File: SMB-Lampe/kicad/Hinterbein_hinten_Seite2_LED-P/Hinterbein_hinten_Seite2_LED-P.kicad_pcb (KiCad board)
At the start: 2 copper layers, 13.3 x 39.6 mm, 6 parts, among them J1 Conn_01x01_Pin

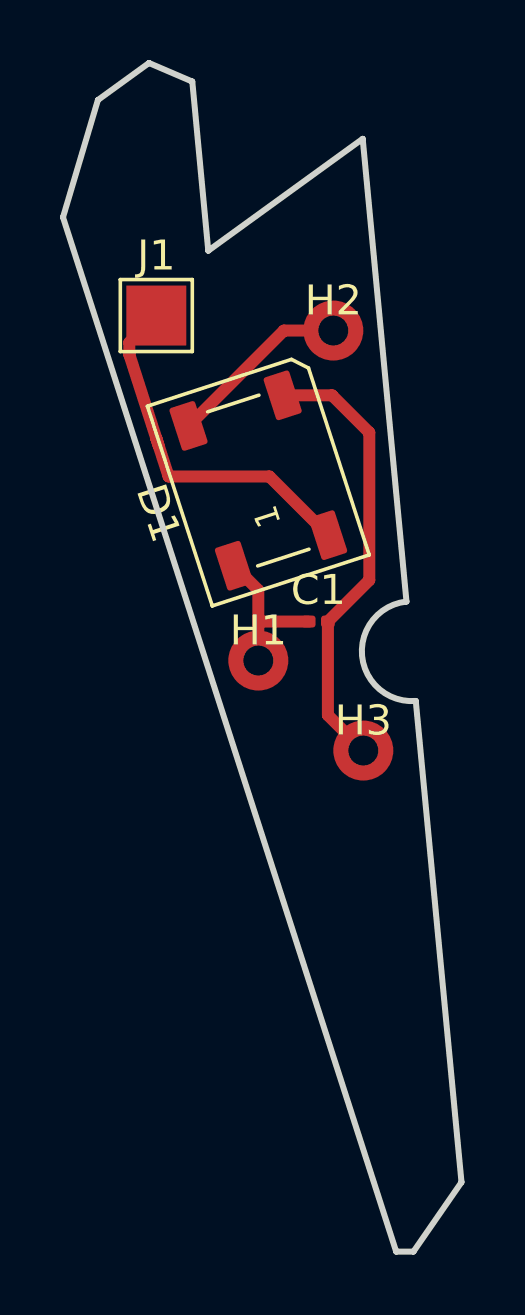
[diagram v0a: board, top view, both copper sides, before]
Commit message: Vorderes Hinterbein fertig
Alle Platinen sind fertig beschaltet
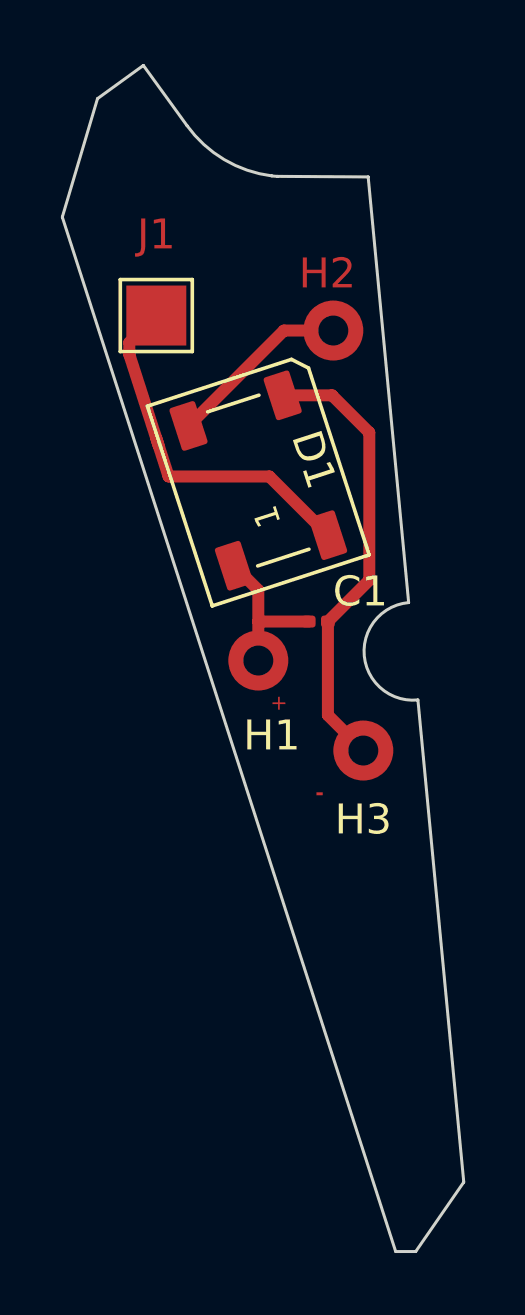
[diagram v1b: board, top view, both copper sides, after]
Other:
- board size 13.3 x 39.6 mm -> 13.4 x 39.5 mm
- board text added: "+"
- board text added: "-"
- board text removed: "108"
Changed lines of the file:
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@@
 		(at 135.5 100.7)
 		(property "Reference" "H3"
-			(at 0 -1 0)
+			(at 0 2.3 0)
 			(unlocked yes)
 			(layer "F.SilkS")
@@
 		(tags "LED RGB NeoPixel PLCC-4 5050")
 		(property "Reference" "D1"
-			(at 0 -3.5 108)
+			(at 0.094058 1.975766 108)
 			(layer "F.SilkS")
 			(effects
@@
 		)
 		(fp_line
-			(start 3.5 2.3)
+			(start 3.5 2.300001)
 			(end 3.5 -2.75)
 			(stroke
@@
 		(fp_line
 			(start 3.05 2.749999)
-			(end 3.5 2.3)
+			(end 3.5 2.300001)
 			(stroke
 				(width 0.12)
@@
 		(at 132 97.7)
 		(property "Reference" "H1"
-			(at 0 -1 0)
+			(at 0.45 2.5 0)
 			(unlocked yes)
 			(layer "F.SilkS")
@@
 		(at 134.5 86.7)
 		(property "Reference" "H2"
-			(at 0 -1 0)
-			(unlocked yes)
-			(layer "F.SilkS")
+			(at -0.2 -1.9 0)
+			(unlocked yes)
+			(layer "F.Cu")
 			(effects
 				(font
@@
 		(tags "test point SMD pad rectangle square")
 		(property "Reference" "J1"
-			(at 0 -1.998 0)
-			(layer "F.SilkS")
+			(at 0 -2.7 0)
+			(layer "F.Cu")
 			(effects
 				(font
@@
 		(tags "capacitor")
 		(property "Reference" "C1"
-			(at 0 -1.05 0)
+			(at 1.4 -1 0)
 			(layer "F.SilkS")
 			(effects
@@
 		)
 	)
-	(gr_line
-		(start 130.331995 84.039152)
-		(end 129.8 78.4)
-		(stroke
-			(width 0.2)
+	(gr_arc
+		(start 132.450996 81.545317)
+		(mid 130.861045 81.000051)
+		(end 129.620705 79.865664)
+		(stroke
+			(width 0.1)
 			(type default)
 		)
@@
 	)
 	(gr_line
-		(start 125.489765 82.924183)
-		(end 136.595866 117.402629)
-		(stroke
-			(width 0.2)
+		(start 137.247196 117.399211)
+		(end 138.848769 115.086383)
+		(stroke
+			(width 0.1)
 			(type default)
 		)
@@
 	)
 	(gr_line
-		(start 136.939186 95.734062)
-		(end 135.479885 80.308378)
-		(stroke
-			(width 0.2)
+		(start 135.66241 81.579414)
+		(end 132.639039 81.560817)
+		(stroke
+			(width 0.1)
 			(type default)
 		)
@@
 	)
 	(gr_line
-		(start 138.773216 115.088786)
-		(end 137.24916 99.046738)
-		(stroke
-			(width 0.2)
+		(start 125.4669 82.917568)
+		(end 136.578951 117.399712)
+		(stroke
+			(width 0.1)
 			(type default)
 		)
@@
 	)
 	(gr_line
-		(start 136.595866 117.402629)
-		(end 137.172273 117.402198)
-		(stroke
-			(width 0.2)
+		(start 136.578951 117.399712)
+		(end 137.247196 117.399211)
+		(stroke
+			(width 0.1)
 			(type default)
 		)
@@
 	)
 	(gr_line
-		(start 137.172273 117.402198)
-		(end 138.773216 115.088786)
-		(stroke
-			(width 0.2)
+		(start 128.1687 77.862122)
+		(end 126.64 78.97)
+		(stroke
+			(width 0.1)
 			(type default)
 		)
 		(layer "Edge.Cuts")
 	)
+	(gr_line
+		(start 126.64 78.97)
+		(end 125.4669 82.917568)
+		(stroke
+			(width 0.1)
+			(type default)
+		)
+		(layer "Edge.Cuts")
+	)
 	(gr_arc
-		(start 137.24916 99.046738)
-		(mid 135.45875 97.54343)
-		(end 136.939186 95.734062)
-		(stroke
-			(width 0.2)
+		(start 132.639039 81.560817)
+		(mid 132.544851 81.555086)
+		(end 132.450996 81.545317)
+		(stroke
+			(width 0.1)
 			(type default)
 		)
@@
 	)
 	(gr_line
-		(start 128.355942 77.781719)
-		(end 126.653074 79.016283)
-		(stroke
-			(width 0.2)
+		(start 137.011642 95.767608)
+		(end 135.66241 81.579414)
+		(stroke
+			(width 0.1)
 			(type default)
 		)
 		(layer "Edge.Cuts")
 	)
-	(gr_line
-		(start 126.653074 79.016283)
-		(end 125.489765 82.924183)
-		(stroke
-			(width 0.2)
+	(gr_arc
+		(start 137.320284 99.013214)
+		(mid 135.531923 97.545801)
+		(end 137.011642 95.767608)
+		(stroke
+			(width 0.1)
 			(type default)
 		)
@@
 	)
 	(gr_line
-		(start 129.8 78.4)
-		(end 128.355942 77.781719)
-		(stroke
-			(width 0.2)
+		(start 129.620705 79.865664)
+		(end 128.1687 77.862122)
+		(stroke
+			(width 0.1)
 			(type default)
 		)
@@
 	)
 	(gr_line
-		(start 135.479885 80.308378)
-		(end 130.331995 84.039152)
-		(stroke
-			(width 0.2)
+		(start 138.848769 115.086383)
+		(end 137.320284 99.013214)
+		(stroke
+			(width 0.1)
 			(type default)
 		)
@@
 		(layer "User.4")
 	)
-	(gr_text "108\n"
-		(at 141.8 93.4 0)
-		(layer "User.4")
+	(gr_text "+"
+		(at 132.4 99.4 0)
+		(layer "F.Cu")
 		(effects
 			(font
-				(size 1 1)
-				(thickness 0.15)
+				(size 0.5 0.5)
+				(thickness 0.1)
+			)
+			(justify left bottom)
+		)
+	)
+	(gr_text "-"
+		(at 133.9 102.4 0)
+		(layer "F.Cu")
+		(effects
+			(font
+				(size 0.5 0.5)
+				(thickness 0.125)
+				(bold yes)
 			)
 			(justify left bottom)
@@
 	)
 	(segment
-		(start 128.603878 90.30548)
-		(end 128.603117 90.304719)
-		(width 0.4)
-		(layer "F.Cu")
-		(net 3)
-	)
-	(segment
 		(start 127.700139 87.499859)
 		(end 128.671646 90.515863)
@@
 	)
 	(group ""
-		(members "10cfd15d-5a2e-4dda-892e-2182e641c5f0" "1f3f11d6-0e22-41ce-9a94-7e0ba691d4ad"
-			"41e3baba-942e-4cf1-b0a5-94dc169ff290" "7841008e-2eb8-48ec-95b5-ab771af922be"
-			"7c0b74bc-bd77-493a-bde5-9f8fa034662b" "8741009e-52f9-408e-9396-0362df0280eb"
-			"9e2b354f-5e23-4003-b19e-7c157c485098" "cffc282a-04d3-4179-b1ed-3f6810a5406e"
-			"d4bc821e-9c93-4e21-9f6a-b7d0490f9b58" "ec7a140b-7b6b-46b3-b898-946da20779df"
-			"f2383213-d998-4c53-9149-38cc7e93ebbe"
-		)
-	)
+		(members "0efc95af-193c-49d2-9e09-1a8f69c3bb3d" "16a32319-458c-438e-b171-7729371724ec"
+			"2210d29f-9bd6-4a4b-b52f-18df89c2af68" "464553f2-b5a1-4726-8af0-7a3ac4ca2adf"
+			"4b9f3d37-edfc-4de5-b353-923798e711a8" "715f1431-12bb-4a99-90ad-165a376b2e6d"
+			"b8cf2599-00b0-491a-b27d-4d2f49a2463f" "c21f45ba-7cce-4116-9ba6-b60ac0a836e1"
+			"d64fb378-59a9-41b0-bc02-83350f69bb6b" "d905b942-e3d8-4b2c-8f38-79aaf0d43560"
+			"ee67463b-4829-4358-ba90-b453c7e6591d" "f9e5fbe0-5104-4c15-98bc-94913d0f390d"
+		)
+	)

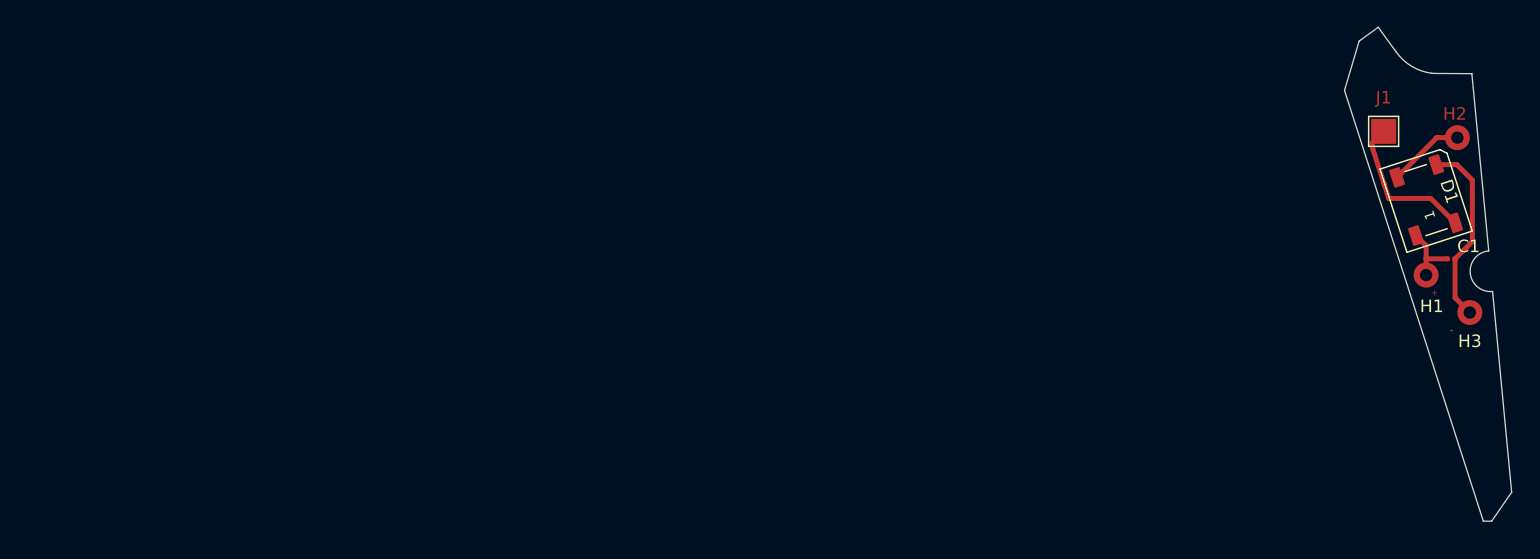
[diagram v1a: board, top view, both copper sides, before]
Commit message: Hinterbeine Geändert teilweiße Körper
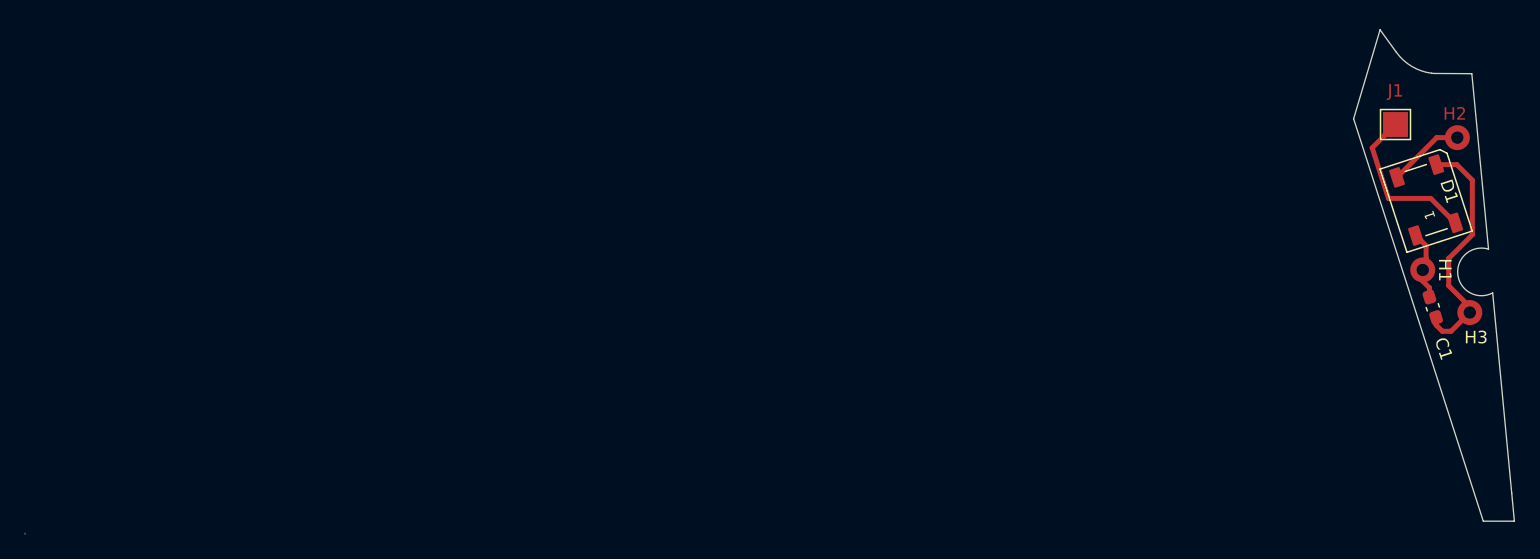
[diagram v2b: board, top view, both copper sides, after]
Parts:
- C1: footprint Capacitor_SMD:C_0201_0603Metric -> Capacitor_SMD:C_0603_1608Metric_Pad1.08x0.95mm_HandSolder
- moved C1 4.15 mm to (132.5, 100.3), turned to -72 degrees
- moved J1 1.10 mm to (129.6, 85.7)
- moved H1 0.49 mm to (131.7, 97.3)
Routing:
- net GND: track 15.1 -> 19.6 mm
- net /Data_OUT_Körper_Seite1: track 12.3 -> 14.3 mm
- net /+5V_IN_Hinterbein_hinten_Seite1: track 5.18 -> 5.89 mm
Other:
- board size 13.4 x 39.5 mm -> 119.2 x 40.3 mm
- board text removed: "+"
- board text removed: "-"

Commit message: Alle Platinen sind fertig zur Fertigung
Aus diesem Stand folgt das erste fertig leuchtende Pferd
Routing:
- net (no net): track 0.00 -> 0.55 mm
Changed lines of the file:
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@@
 		(tenting front back)
 		(pcbplotparams
-			(layerselection 0x00000000_00000000_55555555_5755f5ff)
+			(layerselection 0x00000000_00000000_55555555_57555551)
 			(plot_on_all_layers_selection 0x00000000_00000000_00000000_00000000)
 			(disableapertmacros no)
@@
 			(outputformat 1)
 			(mirror no)
-			(drillshape 1)
+			(drillshape 0)
 			(scaleselection 1)
-			(outputdirectory "")
+			(outputdirectory "fräsen/")
 		)
 	)
@@
 			(at -0.2 -1.9 0)
 			(unlocked yes)
-			(layer "F.Cu")
+			(layer "F.SilkS")
 			(effects
 				(font
@@
 		(property "Reference" "J1"
 			(at 0 -2.7 0)
-			(layer "F.Cu")
+			(layer "F.SilkS")
 			(effects
 				(font
@@
 	)
 	(segment
+		(start 135.27 102.29)
+		(end 135.82 102.29)
+		(width 0.2)
+		(layer "F.Cu")
+		(net 0)
+	)
+	(segment

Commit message: Nachträgliche Änderungen für die Fertigung und Präsentation
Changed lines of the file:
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@@
 		(tags "LED RGB NeoPixel PLCC-4 5050")
 		(property "Reference" "D1"
-			(at 0.094058 1.975766 108)
+			(at 1.165273 3.533007 108)
 			(layer "F.SilkS")
 			(effects
